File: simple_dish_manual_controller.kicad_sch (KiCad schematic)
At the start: 29 parts, among them J1 Screw_Terminal_01x02, J2 M1_CONNECTOR, J3 M2_CONNECTOR, SW1 SW_SPST, SW2 Pulse Enable, SW3 Pulse Enable, U1 AMS1117-5.0, U2 SN74LVC2G157DCUR, U3 ICM7555xP, U4 SN74LVC2G157DCUR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

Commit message: Simple changes
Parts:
- removed C3, C6: 100n, symbol Device:C_Small
- removed U2, U4: SN74LVC2G157DCUR, Custom_Mux_Switches_Decoders:VSSOP-8_L2.3-W2.0-P0.50-LS3.1-BL, symbol Custom_Switches_Mux_Decoders:SN74LVC2G157DCUR
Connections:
- net OUT_PWM_M1 is gone; now on net OUT_M1: U3.3 (Q)
- net OUT_PWM_M2 is gone; now on net OUT_M2: U5.3 (Q)
- net DIRECTION_M1: now also SW2.4 (A)
- net PULSE_ENABLE_M1: now also SW2.1 (A)
- no-connect marks 10 -> 4
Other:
- note added: "From ISV57T Manual - Suggested Pulse and Dir connection using just a PNP. But the 5V output from the PWM should be sufficient, so skipping the PNP for this design."
- note removed: "A/B = 0 --> Y = A (GND) A/B = 1 --> Y = B (PWM M1)"
- note removed: "A/B = 0 --> Y = A (GND) A/B = 1 --> Y = B (PWM M2)"
- note removed: "Multiplexor selector M2"
- moved on the sheet: J2, J3

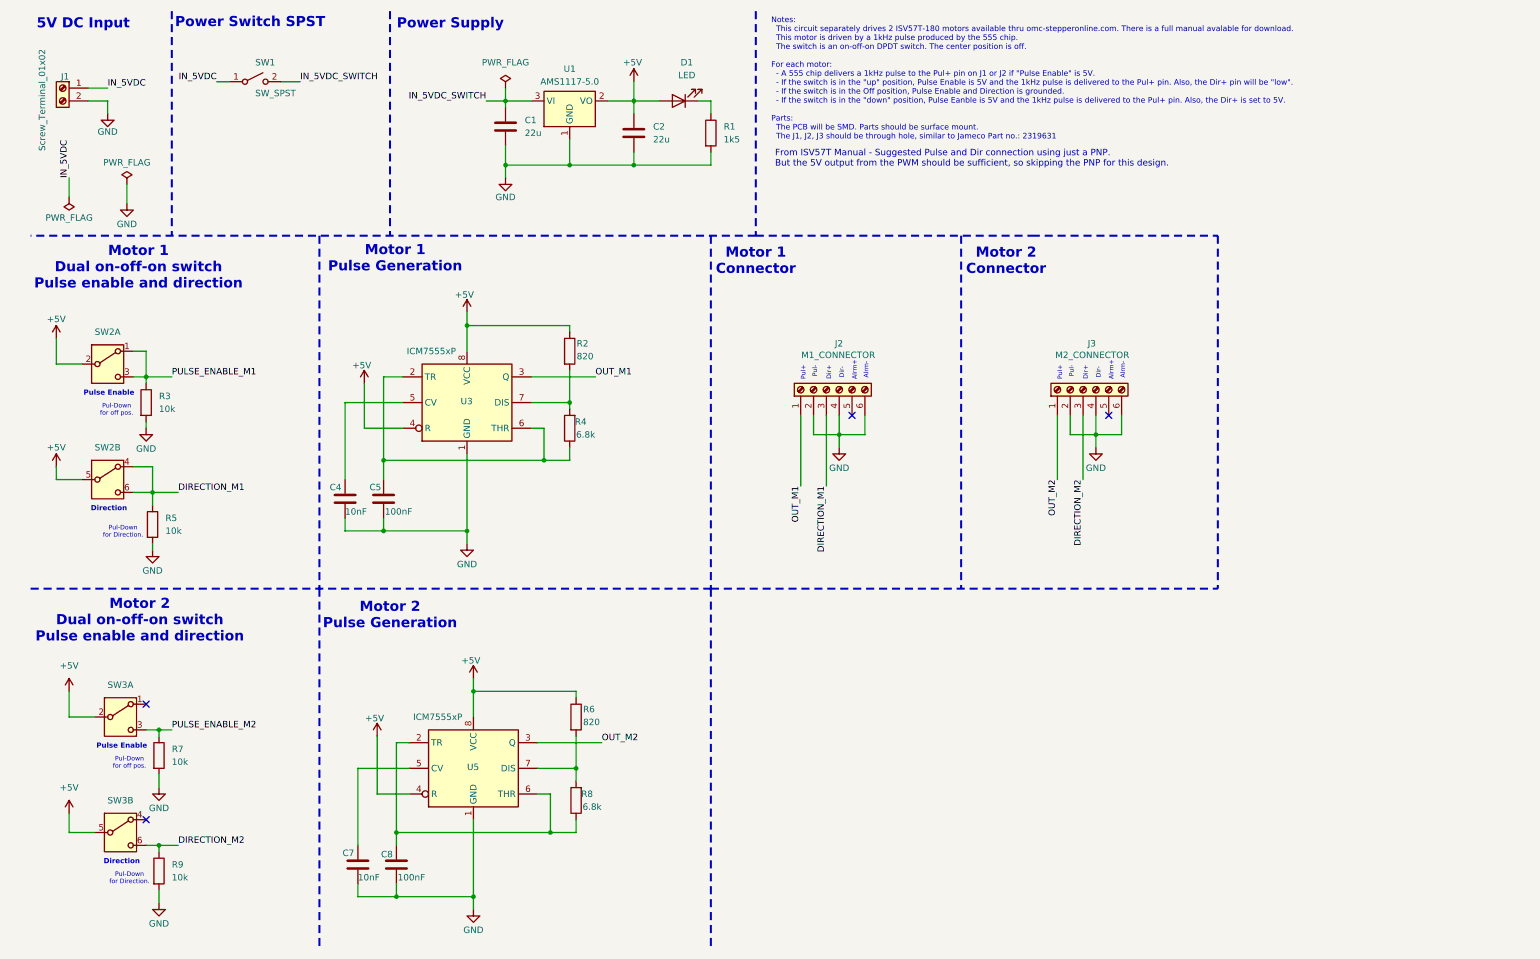
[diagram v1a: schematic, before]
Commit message: Breaking up into sheets
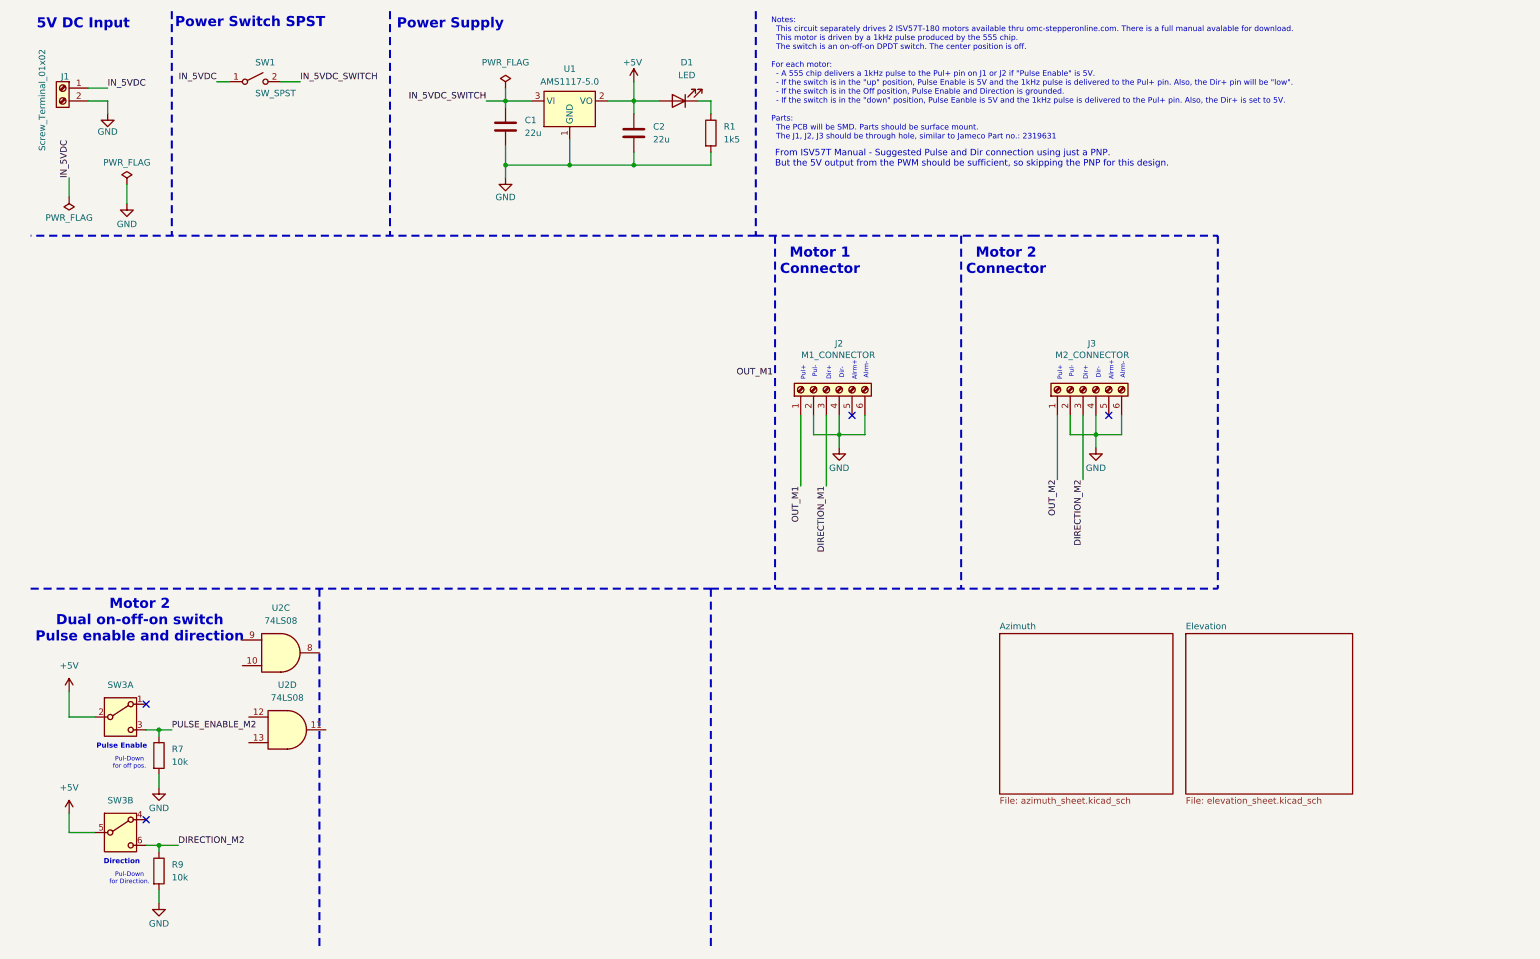
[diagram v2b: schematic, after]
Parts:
- removed C4, C7: 10nF, symbol Device:C
- removed C5, C8: 100nF, symbol Device:C
- removed R2, R6: 820, symbol Device:R
- removed R3, R5: 10k, symbol Device:R
- removed R4, R8: 6.8k, symbol Device:R
- removed SW2: Pulse Enable, symbol Switch:SW_DPDT_x2
- removed U3, U5: ICM7555xP, Package_DIP:DIP-8_W7.62mm, symbol Timer:ICM7555xP
- added U2: 74LS08, symbol 74xx:74LS08
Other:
- added sheet Azimuth (azimuth_sheet.kicad_sch)
- added sheet Elevation (elevation_sheet.kicad_sch)
- note removed: "Motor 1 Dual on-off-on switch Pulse enable and direction"
- note removed: "Motor 1 Pulse Generation"
- note removed: "Motor 2 Pulse Generation"

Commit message: Elevation sheet mostly complete
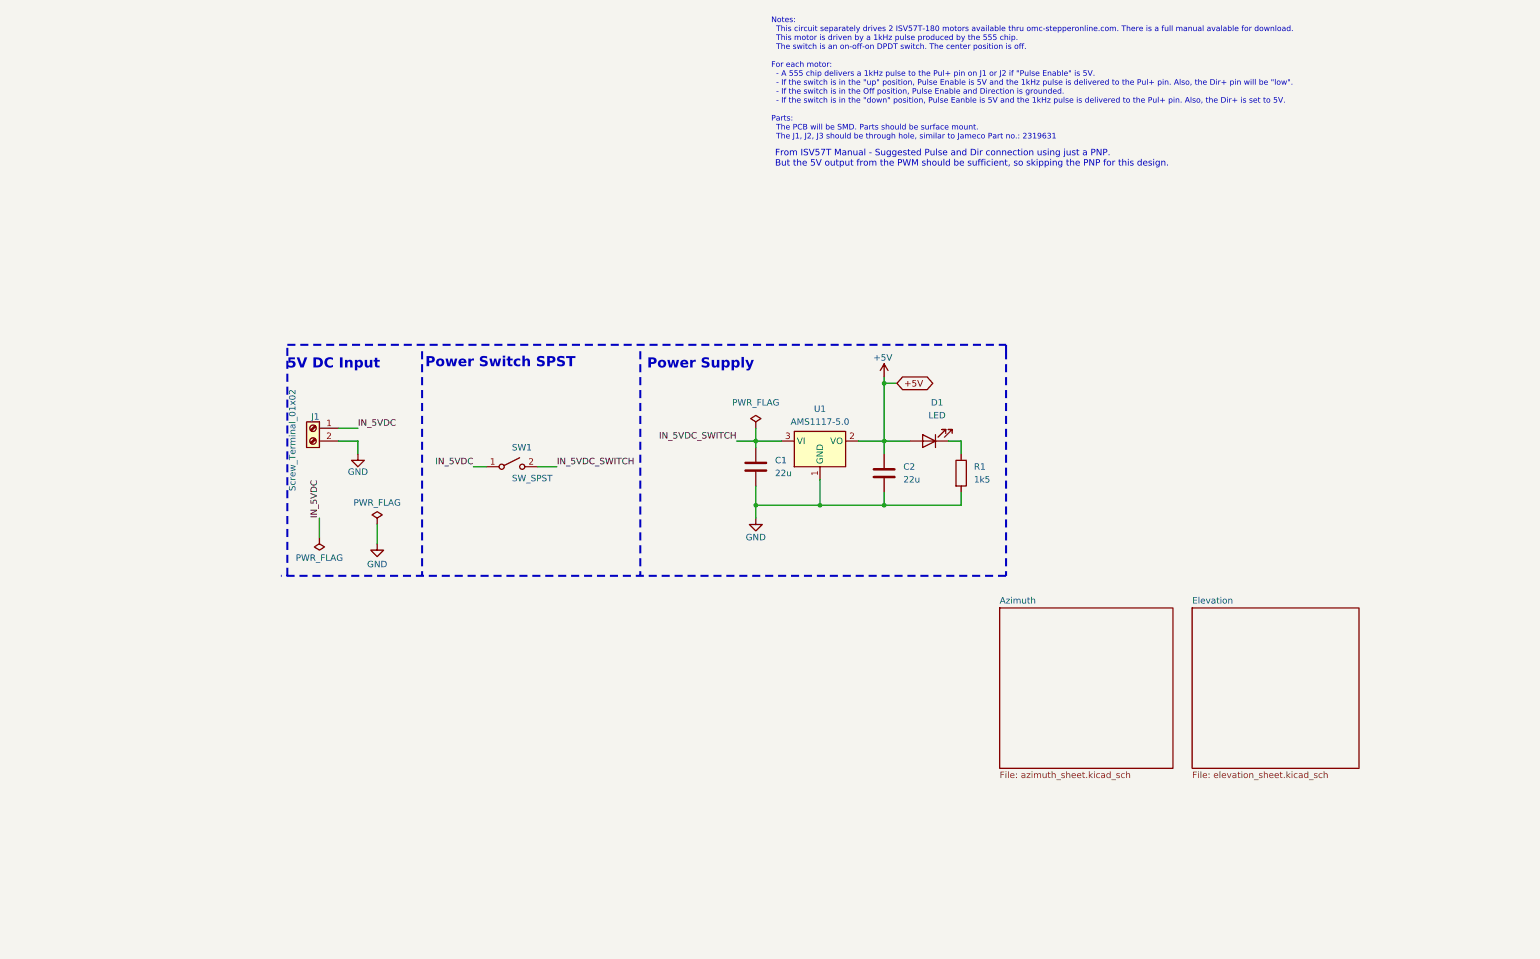
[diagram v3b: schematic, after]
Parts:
- removed J2: M1_CONNECTOR, TerminalBlock_Phoenix:TerminalBlock_Phoenix_MPT-0,5-6-2.54_1x06_P2.54mm_Horizontal, symbol Connector:Screw_Terminal_01x06
- removed J3: M2_CONNECTOR, TerminalBlock_Phoenix:TerminalBlock_Phoenix_MPT-0,5-6-2.54_1x06_P2.54mm_Horizontal, symbol Connector:Screw_Terminal_01x06
- removed R7, R9: 10k, symbol Device:R
- removed SW3: Pulse Enable, symbol Switch:SW_DPDT_x2
- removed U2: 74LS08, symbol 74xx:74LS08
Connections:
- no-connect marks 4 -> 0
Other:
- note removed: "Alrm+"
- note removed: "Alrm-"
- note removed: "Dir+"
- note removed: "Dir-"
- note removed: "Direction"
- note removed: "Motor 1 Connector"
- note removed: "Motor 2 Connector"
- note removed: "Motor 2 Dual on-off-on switch Pulse enable and direction"
- note removed: "Pul+"
- note removed: "Pul-"
- note removed: "Pul-Down for Direction."
- note removed: "Pul-Down for off pos."
- note removed: "Pulse Enable"
- moved on the sheet: C1, C2, D1, J1, R1, SW1, U1

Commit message: Added Azimuth
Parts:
- C1: footprint (none) -> Capacitor_SMD:C_0805_2012Metric
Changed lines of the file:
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@@
 			)
 		)
-		(property "Footprint" ""
+		(property "Footprint" "Capacitor_SMD:C_0805_2012Metric"
 			(at 157.1752 106.68 0)
 			(effects
@@
 		(at 204.47 130.81)
 		(size 34.29 31.75)
-		(exclude_from_sim yes)
-		(in_bom no)
-		(on_board no)
+		(exclude_from_sim no)
+		(in_bom yes)
+		(on_board yes)
 		(dnp no)
 		(fields_autoplaced yes)

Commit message: Latest versions
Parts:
- removed C1: 22u, Capacitor_SMD:C_0805_2012Metric, symbol Device:C
- removed C2: 22u, symbol Device:C
- added C1, C2: 22uF, GRM219R61C226ME15K:CAPC2012X100N, symbol GRM219R61C226ME15K:GRM219R61C226ME15K
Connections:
- net +5V: now also C2.2
- net GND: now also C1.1, C2.1
- net IN_5VDC_SWITCH: now also C1.2
